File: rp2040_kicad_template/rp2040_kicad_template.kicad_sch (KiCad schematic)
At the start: 44 parts

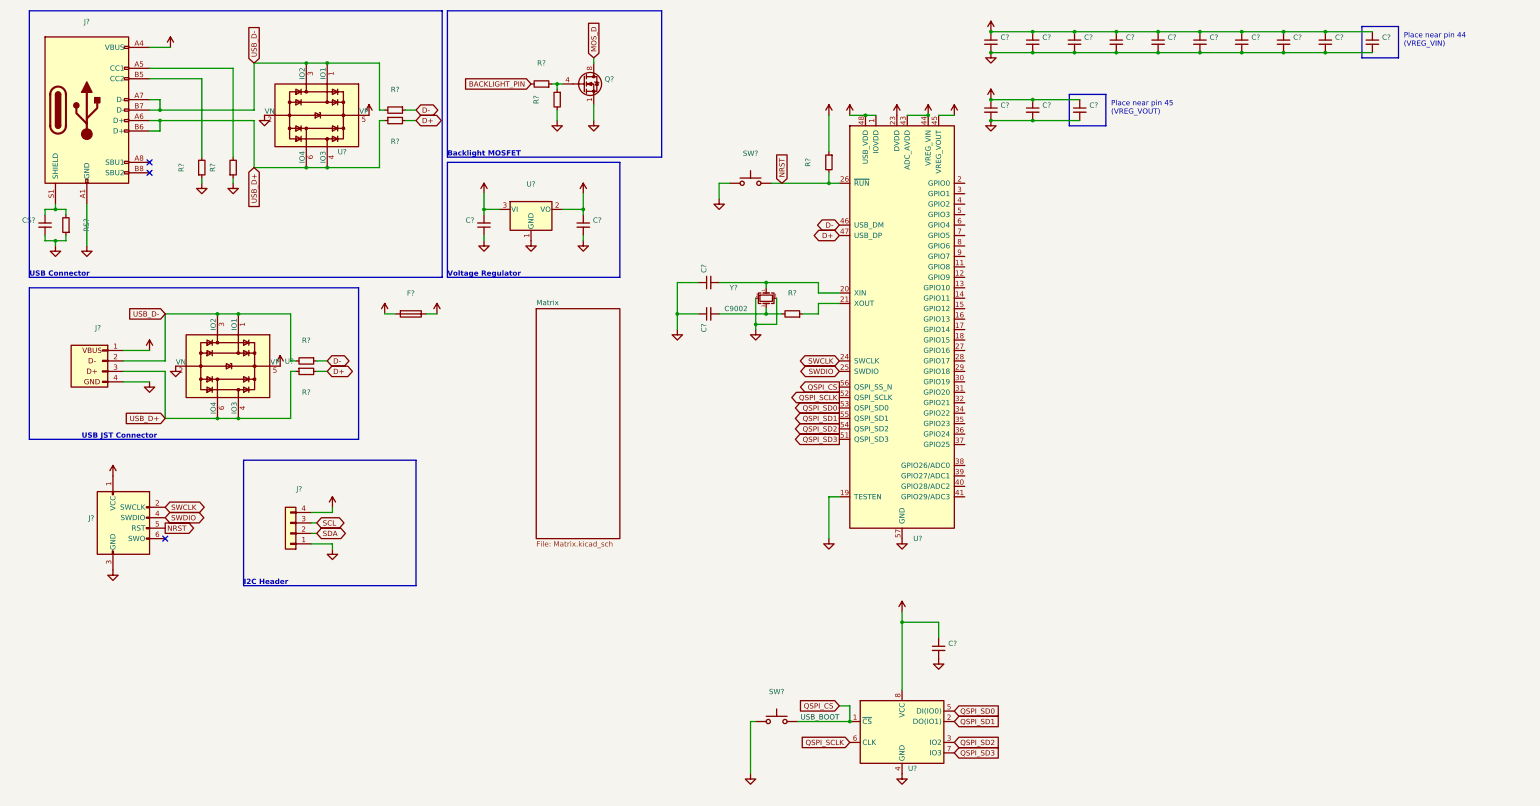
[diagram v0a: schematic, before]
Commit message: Migrate libraries to KiCAD 6
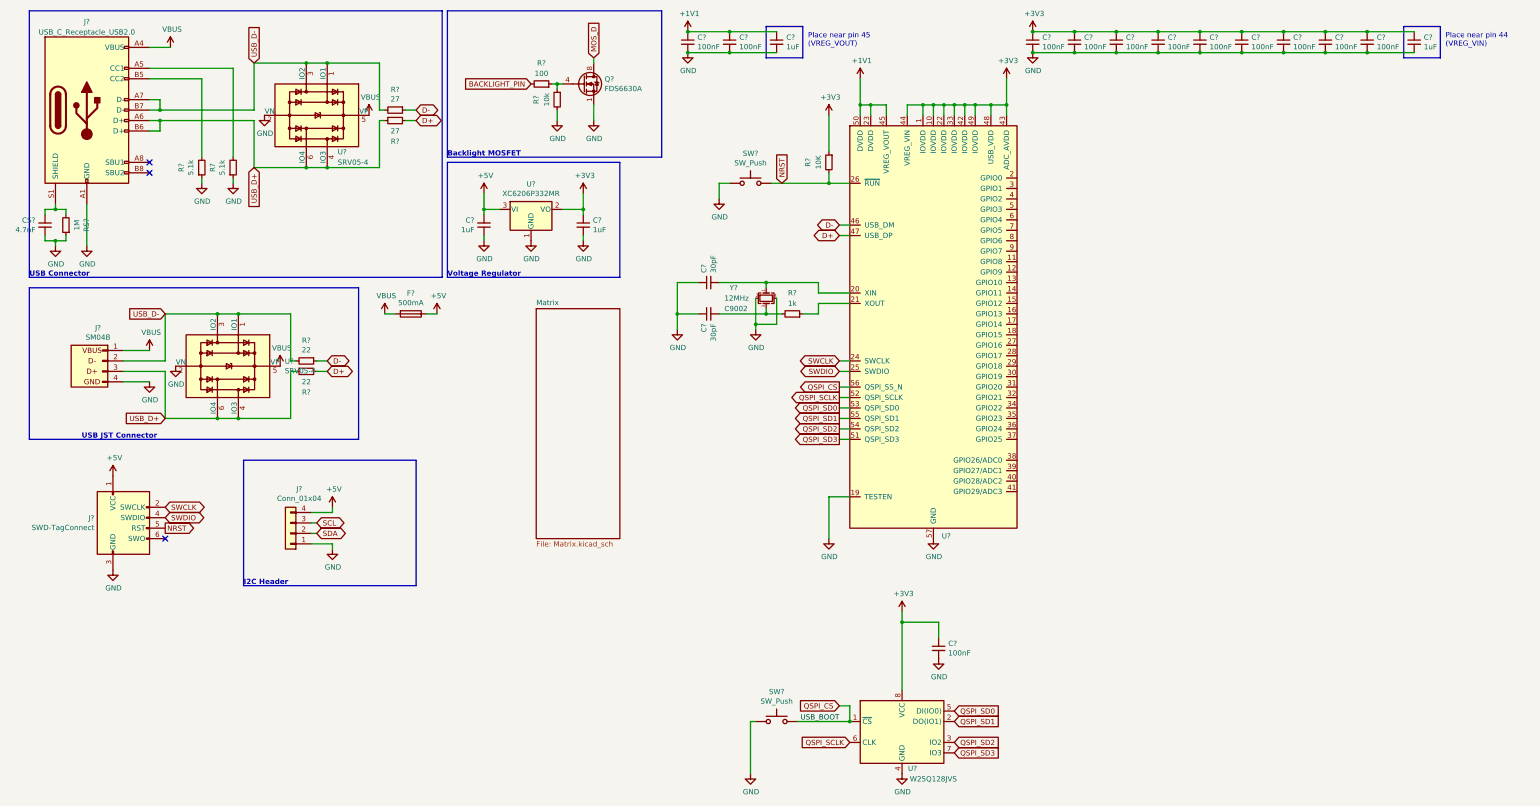
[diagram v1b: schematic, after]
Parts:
- removed U?: (no value), symbol random-keyboard-parts:RP2040
- added U?: (no value), symbol random-keyboard-parts:RP2040
- C? (x2): value (none) -> 30pF; footprint (none) -> Capacitor_SMD:C_0603_1608Metric
- C? (x4): value (none) -> 1uF; footprint (none) -> Capacitor_SMD:C_0603_1608Metric
- C? (x12): value (none) -> 100nF; footprint (none) -> Capacitor_SMD:C_0603_1608Metric
- CS?: value (none) -> 4.7nF; footprint (none) -> Capacitor_SMD:C_0603_1608Metric
- F?: value (none) -> 500mA; footprint (none) -> Fuse:Fuse_1206_3216Metric
- J?: value (none) -> Conn_01x04; footprint (none) -> Connector_JST:JST_SH_SM04B-SRSS-TB_1x04-1MP_P1.00mm_Horizontal
- J?: value (none) -> SM04B; footprint (none) -> Connector_JST:JST_SH_SM04B-SRSS-TB_1x04-1MP_P1.00mm_Horizontal
- J?: value (none) -> SWD-TagConnect; footprint (none) -> Connector:Tag-Connect_TC2030-IDC-NL_2x03_P1.27mm_Vertical
- J?: value (none) -> USB_C_Receptacle_USB2.0
- Q?: value (none) -> FDS6630A; footprint (none) -> Package_SO:SOIC-8_3.9x4.9mm_P1.27mm
- R? (x2): value (none) -> 27; footprint (none) -> Resistor_SMD:R_0603_1608Metric
- R?: value (none) -> 10k; footprint (none) -> Resistor_SMD:R_0603_1608Metric
- R?: value (none) -> 100; footprint (none) -> Resistor_SMD:R_0603_1608Metric
- R? (x2): value (none) -> 5.1k; footprint (none) -> Resistor_SMD:R_0603_1608Metric
- R? (x2): value (none) -> 22; footprint (none) -> Resistor_SMD:R_0603_1608Metric
- R?: value (none) -> 10K; footprint (none) -> Resistor_SMD:R_0603_1608Metric
- R?: value (none) -> 1k; footprint (none) -> Resistor_SMD:R_0603_1608Metric
- RS?: value (none) -> 1M; footprint (none) -> Resistor_SMD:R_0603_1608Metric
- SW? (x2): value (none) -> SW_Push; footprint (none) -> Button_Switch_SMD:SW_SPST_TL3342
- U? (x2): value (none) -> SRV05-4; footprint (none) -> Package_TO_SOT_SMD:SOT-23-6
- U?: value (none) -> W25Q128JVS; footprint (none) -> Package_SO:SOIC-8_5.23x5.23mm_P1.27mm
- U?: value (none) -> XC6206P332MR; footprint (none) -> Package_TO_SOT_SMD:SOT-23
- Y?: value (none) -> 12MHz; footprint (none) -> Crystal:Crystal_SMD_3225-4Pin_3.2x2.5mm
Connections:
- net +1V1: now also U?.23 (DVDD), U?.45 (VREG_VOUT), U?.50 (DVDD)
- net +3V3: now also U?.1 (IOVDD), U?.10 (IOVDD), U?.22 (IOVDD), U?.33 (IOVDD), U?.42 (IOVDD), U?.43 (ADC_AVDD), U?.44 (VREG_VIN), U?.48 (USB_VDD), U?.49 (IOVDD)
- net D+: now also U?.47 (USB_DP)
- net D-: now also U?.46 (USB_DM)
- net GND: now also U?.19 (TESTEN), U?.57 (GND)
- net NRST: now also U?.26 (~{RUN})
- net QSPI_CS: now also U?.56 (QSPI_SS_N)
- net QSPI_SCLK: now also U?.52 (QSPI_SCLK)
- net QSPI_SD0: now also U?.53 (QSPI_SD0)
- net QSPI_SD1: now also U?.55 (QSPI_SD1)
- net QSPI_SD2: now also U?.54 (QSPI_SD2)
- net QSPI_SD3: now also U?.51 (QSPI_SD3)
- net SWCLK: now also U?.24 (SWCLK)
- net SWDIO: now also U?.25 (SWDIO)
- net at C?.2, Y?.1: now also U?.20 (XIN)
- net at R?.1: now also U?.21 (XOUT)
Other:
- moved on the sheet: C?

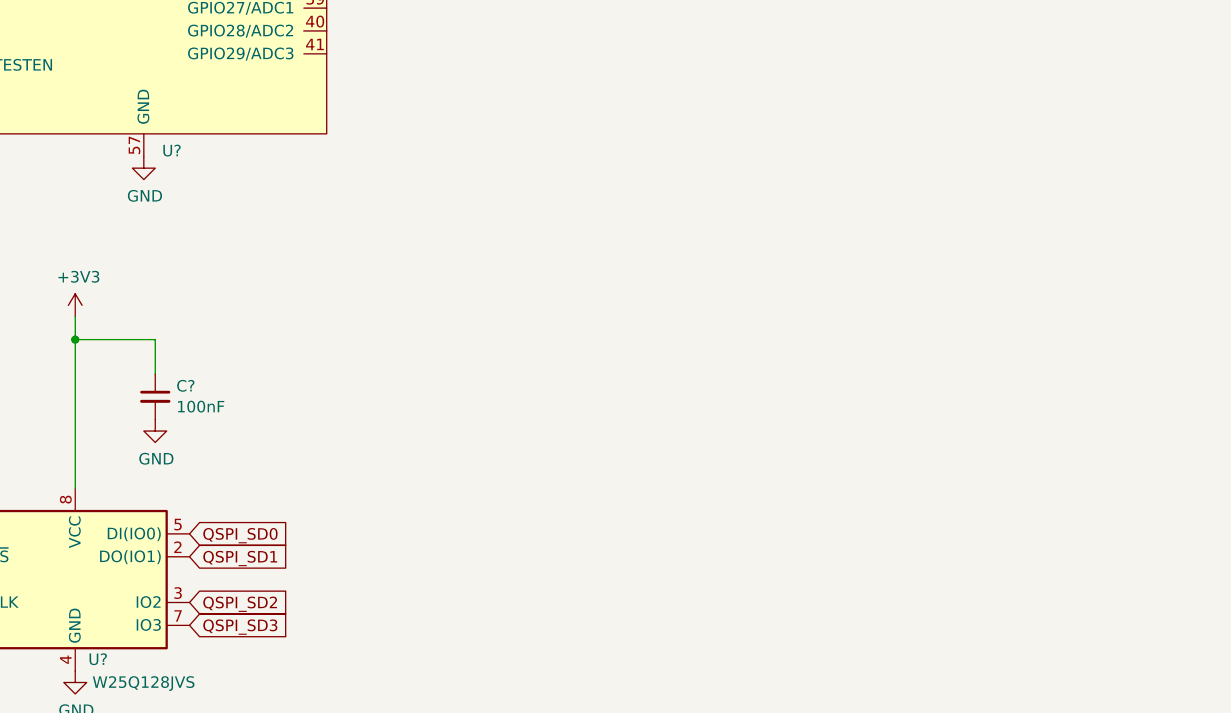
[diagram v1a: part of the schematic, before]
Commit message: Add level shifter to RP2040 template
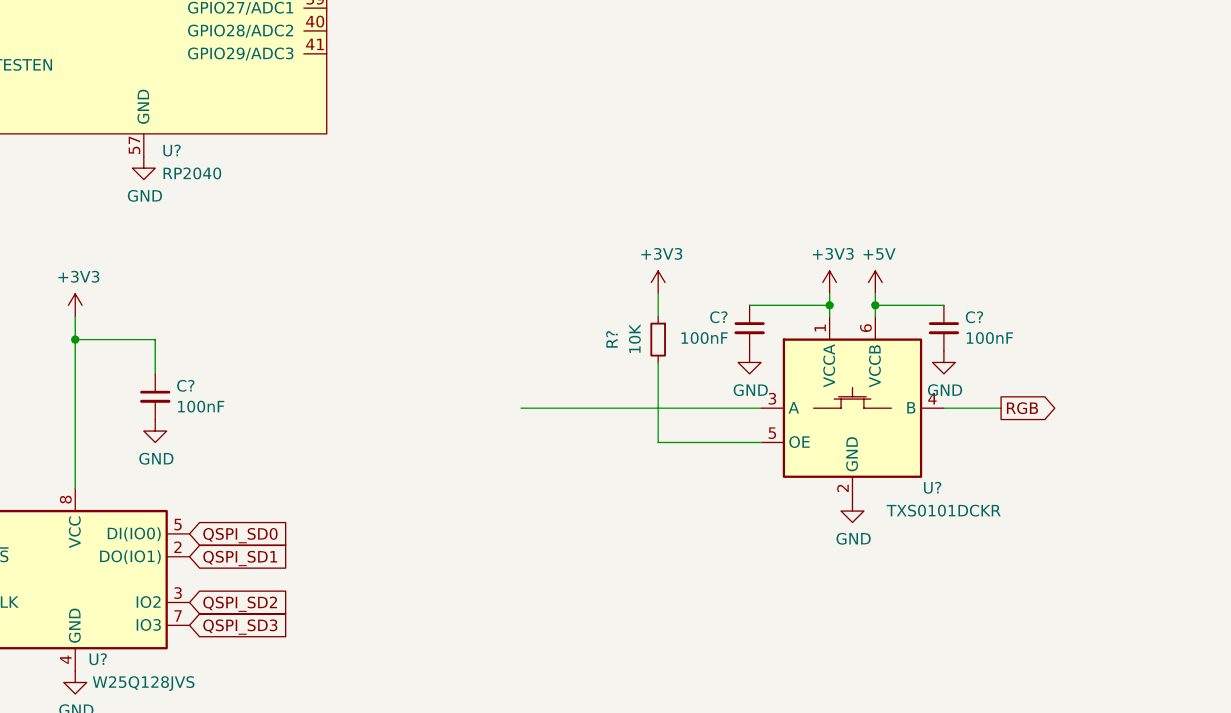
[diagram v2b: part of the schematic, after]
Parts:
- added C? (x2): 100nF, Capacitor_SMD:C_0402_1005Metric, symbol Device:C_Small
- added R?: 10K, symbol Device:R_Small
- added U?: TXS0101DCKR, Package_TO_SOT_SMD:SOT-363_SC-70-6, symbol random-keyboard-parts:TXS0101DCKR
- C? (x14), CS?: footprint Capacitor_SMD:C_0603_1608Metric -> (none)
- R? (x10), RS?: footprint Resistor_SMD:R_0603_1608Metric -> (none)
- U?: value (none) -> RP2040; footprint (none) -> random-keyboard-parts:RP2040-QFN-56
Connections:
- net +3V3: now also C?.1, R?.1, U?.1 (VCCA)
- net +5V: now also C?.1, U?.6 (VCCB)
- net GND: now also C?.2, C?.2, U?.2 (GND)
- new net: R?.2, U?.5 (OE)
- new net RGB: U?.4 (B)
